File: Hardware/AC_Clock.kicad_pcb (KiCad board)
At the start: 2 copper layers, 101.6 x 175.3 mm, 63 parts, among them J1 L, J2 N, J3 Conn_01x10, J4 Conn_01x10, J5 Minutes, J6 Hours, J7 PWR, J8 PWR, Q1 BSS138, SW3 Hour Set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

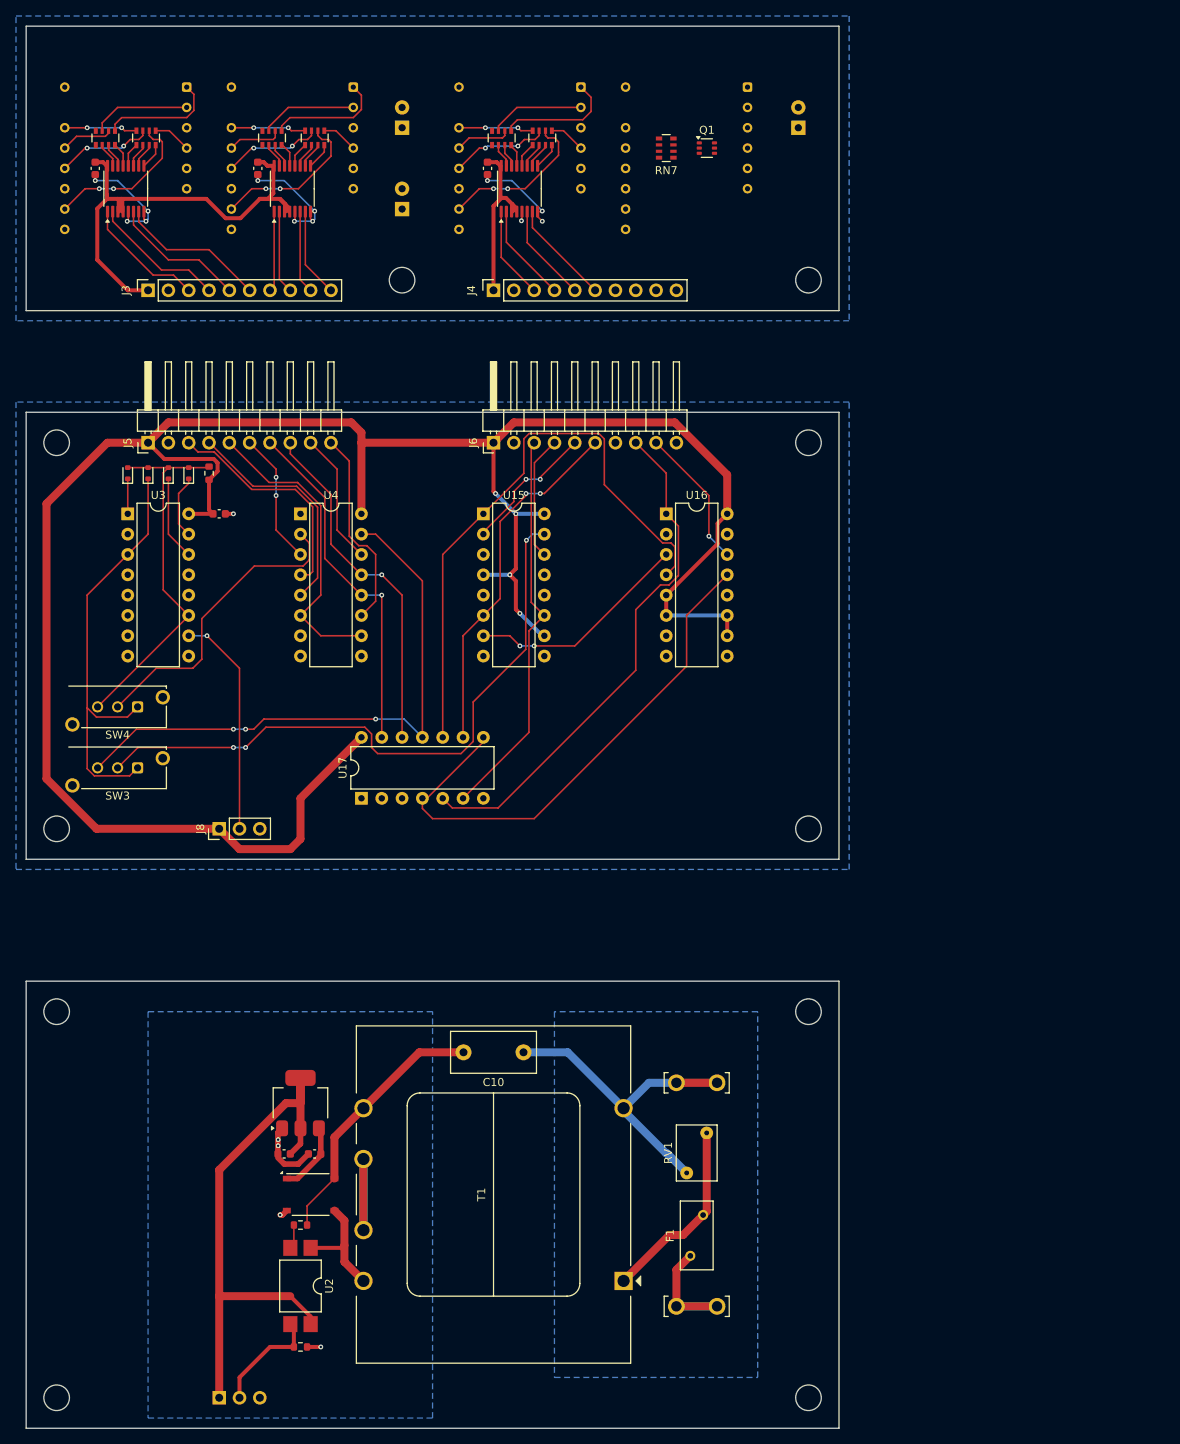
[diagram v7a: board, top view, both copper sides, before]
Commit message: Update board layout to minimize space used
Signed-off-by: Joel Cranmer <42.joel.cranmer@gmail.com>
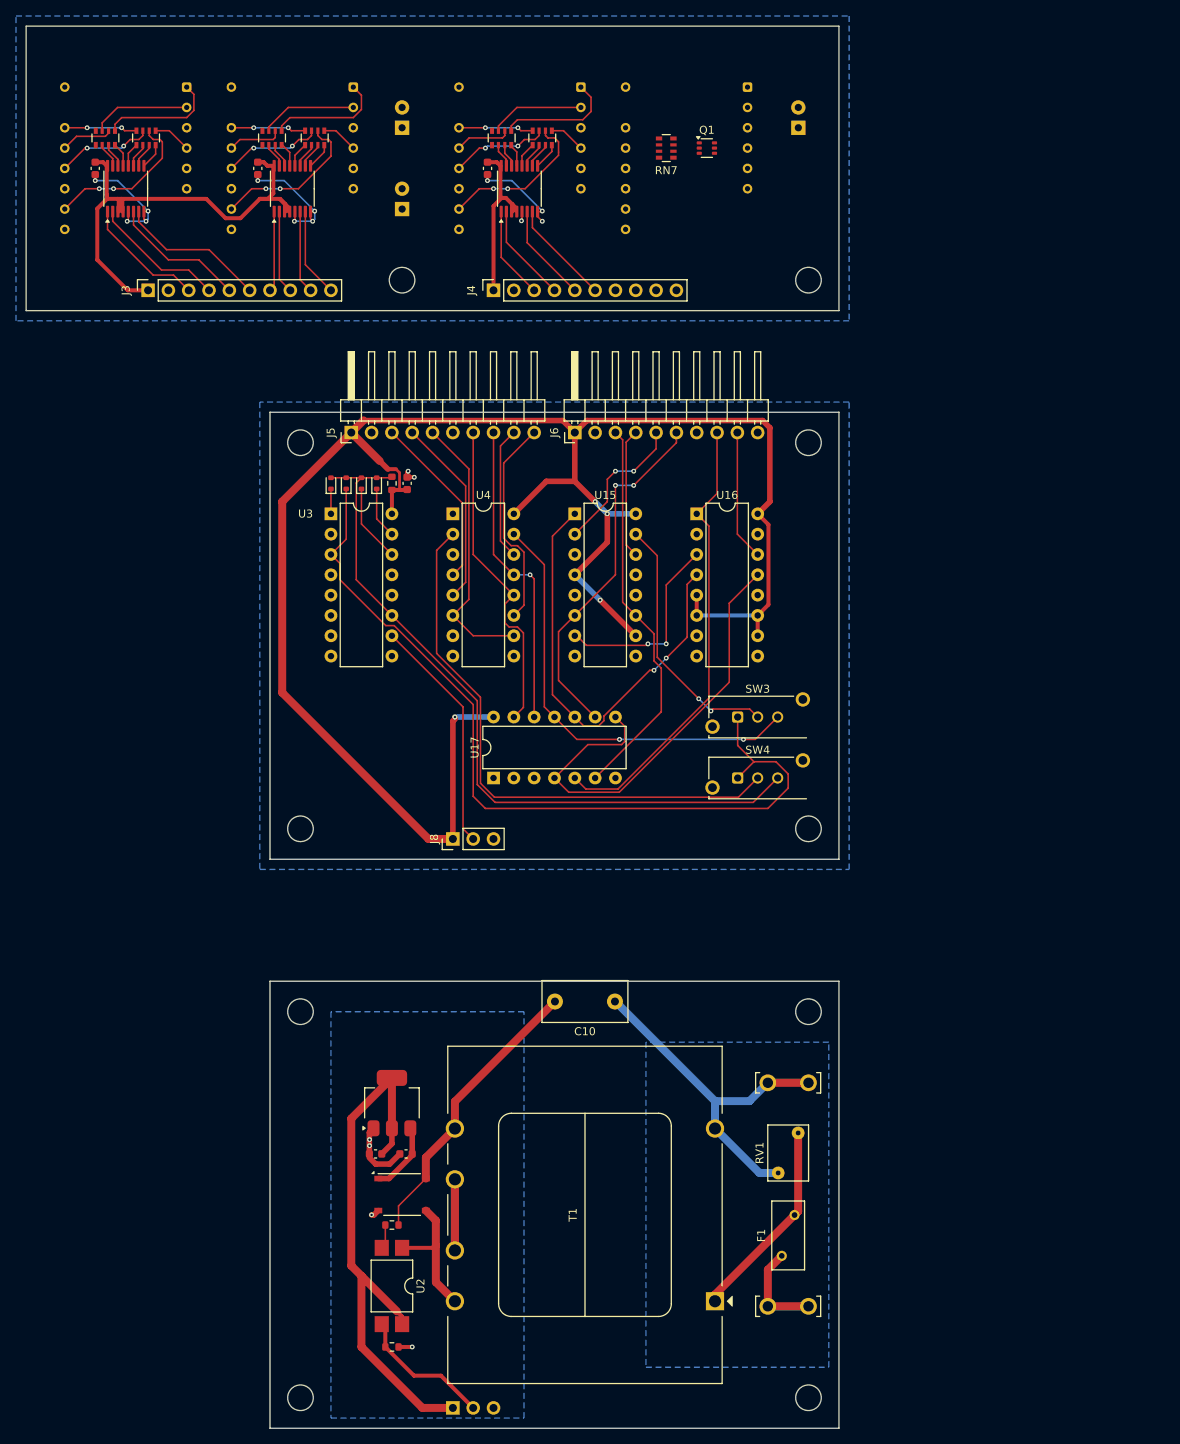
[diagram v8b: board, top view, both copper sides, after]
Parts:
- moved SW4 80.5 mm to (116.8, 119.4), turned to 0 degrees
- moved SW3 80.3 mm to (116.8, 111.8), turned to 0 degrees
- moved REF** 30.5 mm to (59.7, 77.5)
- moved REF** 30.5 mm to (59.7, 148.6)
- moved REF** 30.5 mm to (59.7, 125.7)
- moved REF** 30.5 mm to (59.7, 196.8)
- moved J7 29.2 mm to (78.7, 198.1)
- moved J8 29.2 mm to (78.7, 127.0)
- moved J5 25.4 mm to (66.0, 76.2)
- moved D2 25.4 mm to (63.5, 82.5)
- moved U3 25.4 mm to (63.5, 86.4)
- moved D5 24.8 mm to (65.4, 82.5)
- moved D4 24.2 mm to (67.3, 82.5)
- moved C3 23.8 mm to (73.0, 82.5), turned to 90 degrees
- moved D3 23.5 mm to (69.2, 82.5)
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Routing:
- net /2Hz: track 53.8 -> 104.2 mm
- net /hr: track 80.0 -> 32.3 mm, vias 3 -> 2
- net /minute: track 46.4 -> 92.3 mm
- net +5V: track 425.3 -> 388.3 mm
- net /min: track 38.2 -> 70.6 mm
- net /hour: track 73.7 -> 55.2 mm, vias 3 -> 2
- net Net-(U15-PE): track 73.8 -> 55.4 mm, vias 0 -> 2
- net DA_1: track 35.3 -> 18.7 mm, vias 2 -> 0
- net Net-(U16B-C): track 67.3 -> 57.4 mm
- net /10Hr: track 65.2 -> 56.9 mm
- net DB_1: track 44.1 -> 37.5 mm
- net DC_2: track 54.5 -> 49.3 mm
- net DC_1: track 45.6 -> 40.6 mm
- net /Pulse: track 42.1 -> 46.8 mm, vias 1 -> 0
- net Earth: track 44.9 -> 49.0 mm
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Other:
- outline, holes or cut-outs redrawn
